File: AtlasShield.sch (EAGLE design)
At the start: 7 parts, among them J1 AVR_SPI_PRG_6NS

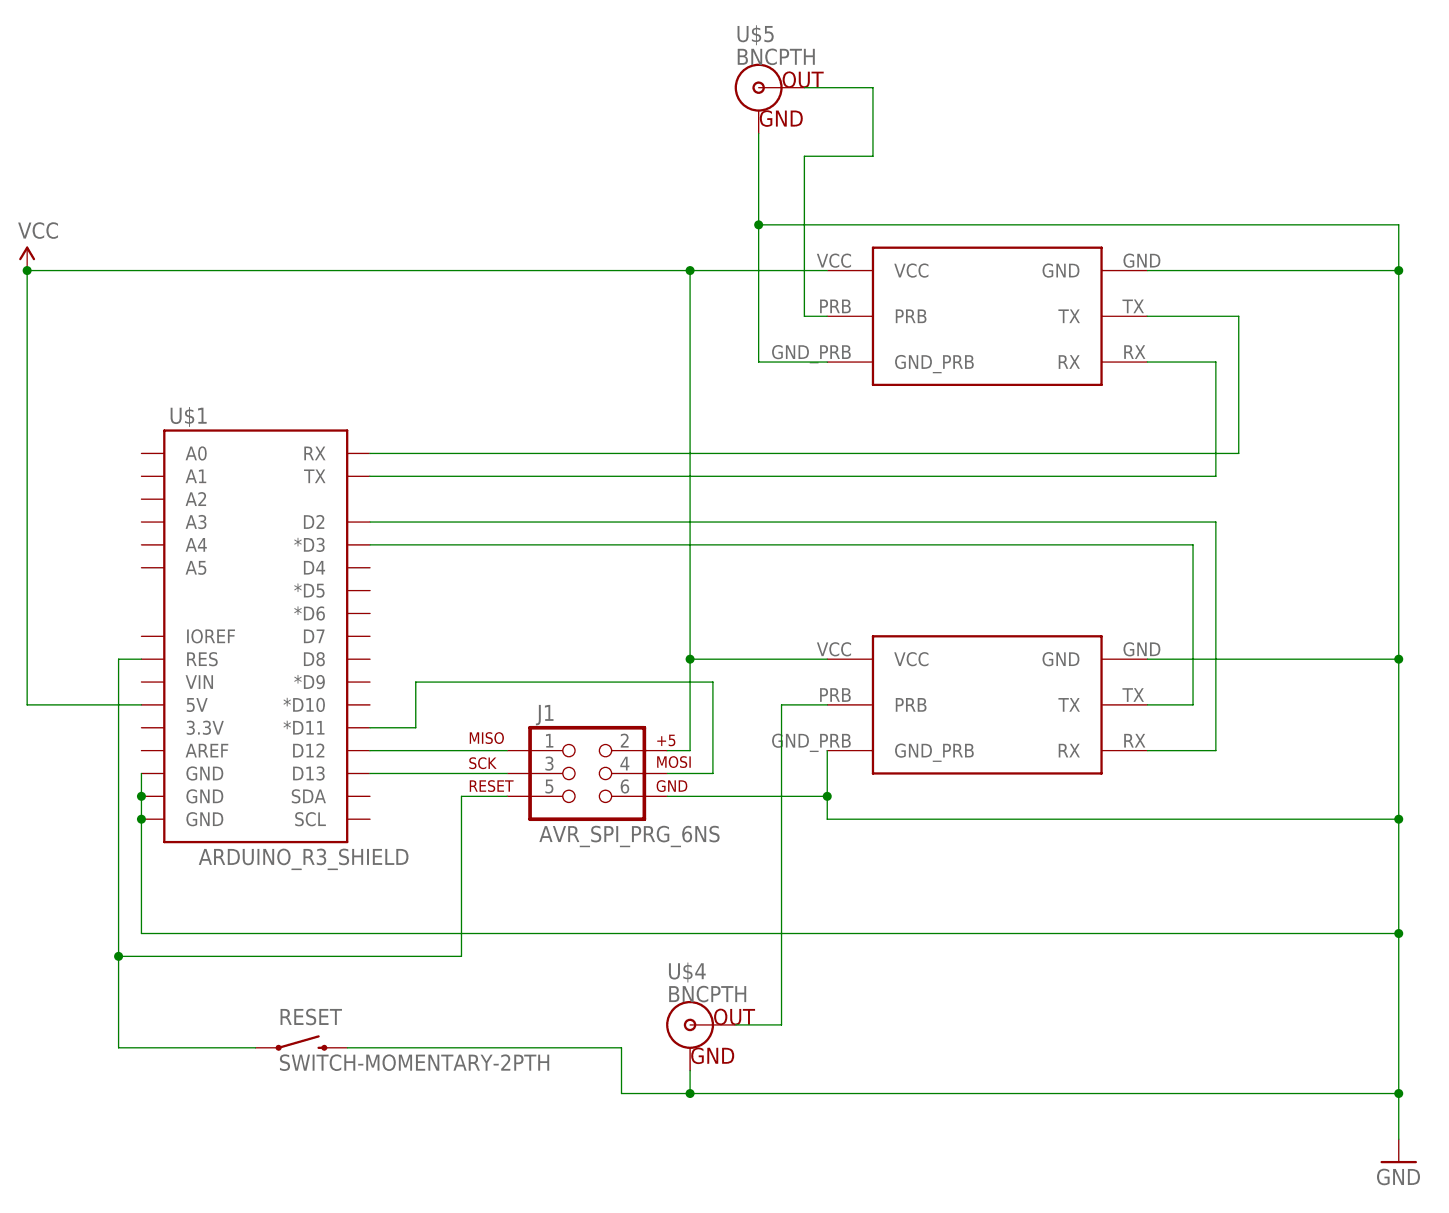
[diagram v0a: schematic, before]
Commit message: added DPDT switches to optionally send either sensor to the SPI bus
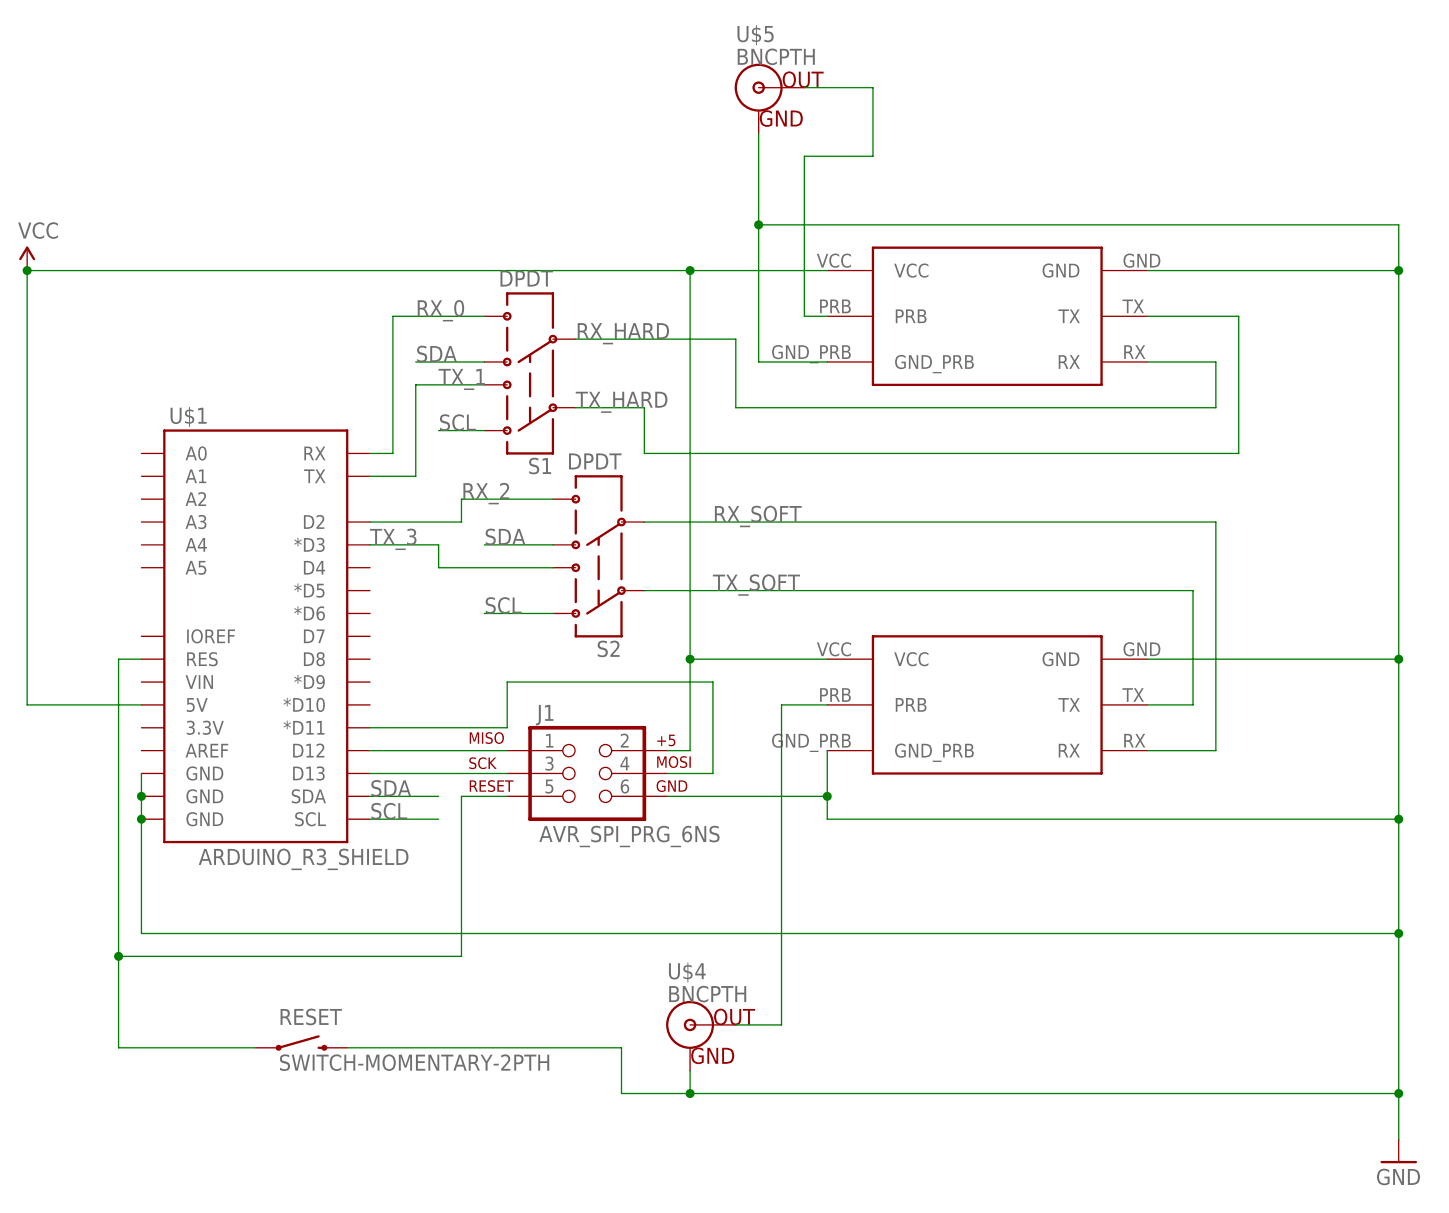
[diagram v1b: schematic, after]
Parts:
- added S1, S2: DPDT, SparkFun-Electromechanical:SWITCH-DPDTAYZ0202
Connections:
- removed net N$1: U$1.RX, U$2.TX
- removed net N$2: U$1.TX, U$2.RX
- removed net N$3: U$1.D2, U$3.RX
- removed net N$4: U$1.*D3, U$3.TX
- new net RX_0: S1.6, U$1.RX
- new net RX_2: S2.6, U$1.D2
- new net RX_HARD: S1.5, U$2.RX
- new net RX_SOFT: S2.5, U$3.RX
- new net SCL: S1.1, S2.1, U$1.SCL
- new net SDA: S1.4, S2.4, U$1.SDA
- new net TX_1: S1.3, U$1.TX
- new net TX_3: S2.3, U$1.*D3
- new net TX_HARD: S1.2, U$2.TX
- new net TX_SOFT: S2.2, U$3.TX
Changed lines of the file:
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@@
 <part name="U$5" library="SparkFun-Connectors" deviceset="BNC" device="PTH"/>
 <part name="RESET" library="SparkFun-Electromechanical" deviceset="SWITCH-MOMENTARY-2" device="PTH"/>
+<part name="S1" library="SparkFun-Electromechanical" deviceset="SWITCH-DPDT" device="AYZ0202" value="DPDT"/>
+<part name="S2" library="SparkFun-Electromechanical" deviceset="SWITCH-DPDT" device="AYZ0202" value="DPDT"/>
 </parts>
 <sheets>
@@
 <instance part="U$5" gate="G$1" x="73.66" y="111.76"/>
 <instance part="RESET" gate="G$1" x="22.86" y="5.08"/>
+<instance part="S1" gate="G$1" x="48.26" y="78.74" rot="R180"/>
+<instance part="S2" gate="G$1" x="55.88" y="58.42" rot="R180"/>
 </instances>
 <busses>
 </busses>
 <nets>
-<net name="N$1" class="0">
-<segment>
-<pinref part="U$1" gate="G$1" pin="RX"/>
-<wire x1="30.48" y1="71.12" x2="127" y2="71.12" width="0.1524" layer="91"/>
+<net name="TX_HARD" class="0">
+<segment>
 <wire x1="127" y1="71.12" x2="127" y2="86.36" width="0.1524" layer="91"/>
 <pinref part="U$2" gate="G$1" pin="TX"/>
 <wire x1="127" y1="86.36" x2="116.84" y2="86.36" width="0.1524" layer="91"/>
-</segment>
-</net>
-<net name="N$2" class="0">
-<segment>
-<pinref part="U$1" gate="G$1" pin="TX"/>
-<wire x1="30.48" y1="68.58" x2="124.46" y2="68.58" width="0.1524" layer="91"/>
-<wire x1="124.46" y1="68.58" x2="124.46" y2="81.28" width="0.1524" layer="91"/>
+<wire x1="127" y1="71.12" x2="60.96" y2="71.12" width="0.1524" layer="91"/>
+<wire x1="60.96" y1="71.12" x2="60.96" y2="76.2" width="0.1524" layer="91"/>
+<pinref part="S1" gate="G$1" pin="2"/>
+<wire x1="60.96" y1="76.2" x2="53.34" y2="76.2" width="0.1524" layer="91"/>
+<label x="53.34" y="76.2" size="1.778" layer="95"/>
+</segment>
+</net>
+<net name="RX_HARD" class="0">
+<segment>
+<wire x1="124.46" y1="76.2" x2="124.46" y2="81.28" width="0.1524" layer="91"/>
 <pinref part="U$2" gate="G$1" pin="RX"/>
 <wire x1="124.46" y1="81.28" x2="116.84" y2="81.28" width="0.1524" layer="91"/>
-</segment>
-</net>
-<net name="N$3" class="0">
-<segment>
-<pinref part="U$1" gate="G$1" pin="D2"/>
-<wire x1="30.48" y1="63.5" x2="124.46" y2="63.5" width="0.1524" layer="91"/>
+<wire x1="124.46" y1="76.2" x2="71.12" y2="76.2" width="0.1524" layer="91"/>
+<wire x1="71.12" y1="76.2" x2="71.12" y2="83.82" width="0.1524" layer="91"/>
+<pinref part="S1" gate="G$1" pin="5"/>
+<wire x1="71.12" y1="83.82" x2="53.34" y2="83.82" width="0.1524" layer="91"/>
+<label x="53.34" y="83.82" size="1.778" layer="95"/>
+</segment>
+</net>
+<net name="RX_SOFT" class="0">
+<segment>
 <wire x1="124.46" y1="63.5" x2="124.46" y2="38.1" width="0.1524" layer="91"/>
 <pinref part="U$3" gate="G$1" pin="RX"/>
 <wire x1="124.46" y1="38.1" x2="116.84" y2="38.1" width="0.1524" layer="91"/>
-</segment>
-</net>
-<net name="N$4" class="0">
-<segment>
-<pinref part="U$1" gate="G$1" pin="*D3"/>
-<wire x1="30.48" y1="60.96" x2="121.92" y2="60.96" width="0.1524" layer="91"/>
-<wire x1="121.92" y1="60.96" x2="121.92" y2="43.18" width="0.1524" layer="91"/>
+<pinref part="S2" gate="G$1" pin="5"/>
+<wire x1="124.46" y1="63.5" x2="60.96" y2="63.5" width="0.1524" layer="91"/>
+<label x="68.58" y="63.5" size="1.778" layer="95"/>
+</segment>
+</net>
+<net name="TX_SOFT" class="0">
+<segment>
+<wire x1="121.92" y1="55.88" x2="121.92" y2="43.18" width="0.1524" layer="91"/>
 <pinref part="U$3" gate="G$1" pin="TX"/>
 <wire x1="121.92" y1="43.18" x2="116.84" y2="43.18" width="0.1524" layer="91"/>
+<pinref part="S2" gate="G$1" pin="2"/>
+<wire x1="121.92" y1="55.88" x2="60.96" y2="55.88" width="0.1524" layer="91"/>
+<label x="68.58" y="55.88" size="1.778" layer="95"/>
 </segment>
 </net>
@@
 <wire x1="63.5" y1="35.56" x2="68.58" y2="35.56" width="0.1524" layer="91"/>
 <wire x1="68.58" y1="35.56" x2="68.58" y2="45.72" width="0.1524" layer="91"/>
-<wire x1="68.58" y1="45.72" x2="35.56" y2="45.72" width="0.1524" layer="91"/>
-<wire x1="35.56" y1="45.72" x2="35.56" y2="40.64" width="0.1524" layer="91"/>
+<wire x1="68.58" y1="45.72" x2="45.72" y2="45.72" width="0.1524" layer="91"/>
+<wire x1="45.72" y1="45.72" x2="45.72" y2="40.64" width="0.1524" layer="91"/>
 <pinref part="U$1" gate="G$1" pin="*D11"/>
-<wire x1="35.56" y1="40.64" x2="30.48" y2="40.64" width="0.1524" layer="91"/>
+<wire x1="45.72" y1="40.64" x2="30.48" y2="40.64" width="0.1524" layer="91"/>
 </segment>
 </net>
@@
 </segment>
 </net>
+<net name="RX_0" class="0">
+<segment>
+<pinref part="U$1" gate="G$1" pin="RX"/>
+<wire x1="30.48" y1="71.12" x2="33.02" y2="71.12" width="0.1524" layer="91"/>
+<wire x1="33.02" y1="71.12" x2="33.02" y2="86.36" width="0.1524" layer="91"/>
+<pinref part="S1" gate="G$1" pin="6"/>
+<wire x1="33.02" y1="86.36" x2="43.18" y2="86.36" width="0.1524" layer="91"/>
+<label x="35.56" y="86.36" size="1.778" layer="95"/>
+</segment>
+</net>
+<net name="TX_1" class="0">
+<segment>
+<pinref part="U$1" gate="G$1" pin="TX"/>
+<wire x1="30.48" y1="68.58" x2="35.56" y2="68.58" width="0.1524" layer="91"/>
+<wire x1="35.56" y1="68.58" x2="35.56" y2="78.74" width="0.1524" layer="91"/>
+<pinref part="S1" gate="G$1" pin="3"/>
+<wire x1="35.56" y1="78.74" x2="43.18" y2="78.74" width="0.1524" layer="91"/>
+<label x="38.1" y="78.74" size="1.778" layer="95"/>
+</segment>
+</net>
+<net name="SDA" class="0">
+<segment>
+<pinref part="U$1" gate="G$1" pin="SDA"/>
+<wire x1="30.48" y1="33.02" x2="38.1" y2="33.02" width="0.1524" layer="91"/>
+<label x="30.48" y="33.02" size="1.778" layer="95"/>
+</segment>
+<segment>
+<pinref part="S1" gate="G$1" pin="4"/>
+<wire x1="43.18" y1="81.28" x2="35.56" y2="81.28" width="0.1524" layer="91"/>
+<label x="35.56" y="81.28" size="1.778" layer="95"/>
+</segment>
+<segment>
+<pinref part="S2" gate="G$1" pin="4"/>
+<wire x1="50.8" y1="60.96" x2="43.18" y2="60.96" width="0.1524" layer="91"/>
+<label x="43.18" y="60.96" size="1.778" layer="95"/>
+</segment>
+</net>
+<net name="SCL" class="0">
+<segment>
+<pinref part="U$1" gate="G$1" pin="SCL"/>
+<wire x1="30.48" y1="30.48" x2="38.1" y2="30.48" width="0.1524" layer="91"/>
+<label x="30.48" y="30.48" size="1.778" layer="95"/>
+</segment>
+<segment>
+<pinref part="S2" gate="G$1" pin="1"/>
+<wire x1="50.8" y1="53.34" x2="43.18" y2="53.34" width="0.1524" layer="91"/>
+<label x="43.18" y="53.34" size="1.778" layer="95"/>
+</segment>
+<segment>
+<pinref part="S1" gate="G$1" pin="1"/>
+<wire x1="43.18" y1="73.66" x2="38.1" y2="73.66" width="0.1524" layer="91"/>
+<label x="38.1" y="73.66" size="1.778" layer="95"/>
+</segment>
+</net>
+<net name="RX_2" class="0">
+<segment>
+<pinref part="S2" gate="G$1" pin="6"/>
+<wire x1="50.8" y1="66.04" x2="40.64" y2="66.04" width="0.1524" layer="91"/>
+<wire x1="40.64" y1="66.04" x2="40.64" y2="63.5" width="0.1524" layer="91"/>
+<wire x1="40.64" y1="63.5" x2="30.48" y2="63.5" width="0.1524" layer="91"/>
+<pinref part="U$1" gate="G$1" pin="D2"/>
+<label x="40.64" y="66.04" size="1.778" layer="95"/>
+</segment>
+</net>
+<net name="TX_3" class="0">
+<segment>
+<pinref part="S2" gate="G$1" pin="3"/>
+<wire x1="50.8" y1="58.42" x2="38.1" y2="58.42" width="0.1524" layer="91"/>
+<wire x1="38.1" y1="58.42" x2="38.1" y2="60.96" width="0.1524" layer="91"/>
+<pinref part="U$1" gate="G$1" pin="*D3"/>
+<wire x1="38.1" y1="60.96" x2="30.48" y2="60.96" width="0.1524" layer="91"/>
+<label x="30.48" y="60.96" size="1.778" layer="95"/>
+</segment>
+</net>
